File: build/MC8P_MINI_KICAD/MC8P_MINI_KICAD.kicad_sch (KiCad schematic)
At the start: 28 parts, among them J1 AudioJack3, SW1 ASSIGN, SW2 ENTER, SW3 PREV, SW4 NEXT, U1 CD74HC4067M

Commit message: production files
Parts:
- added R3, R4, R5, R6: 10k_0402, PCM_4ms_Resistor:R_0603, symbol PCM_4ms_Resistor:10k_0402
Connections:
- net 5V: now also SW1.1, SW2.1, SW3.1, SW4.1
- net ASSIGN: now also SW1.2, R3.1; no longer SW1.1
- net ENTER: now also SW2.2, R4.1; no longer SW2.1
- net GND: now also R3.2, R4.2, R5.2, R6.2; no longer SW1.2, SW2.2, SW3.2, SW4.2
- net NEXT: now also SW4.2, R5.1; no longer SW4.1
- net PREV: now also SW3.2, R6.1; no longer SW3.1
- no-connect marks 9 -> 22
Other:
- moved on the sheet: SW1, SW2, SW3, SW4

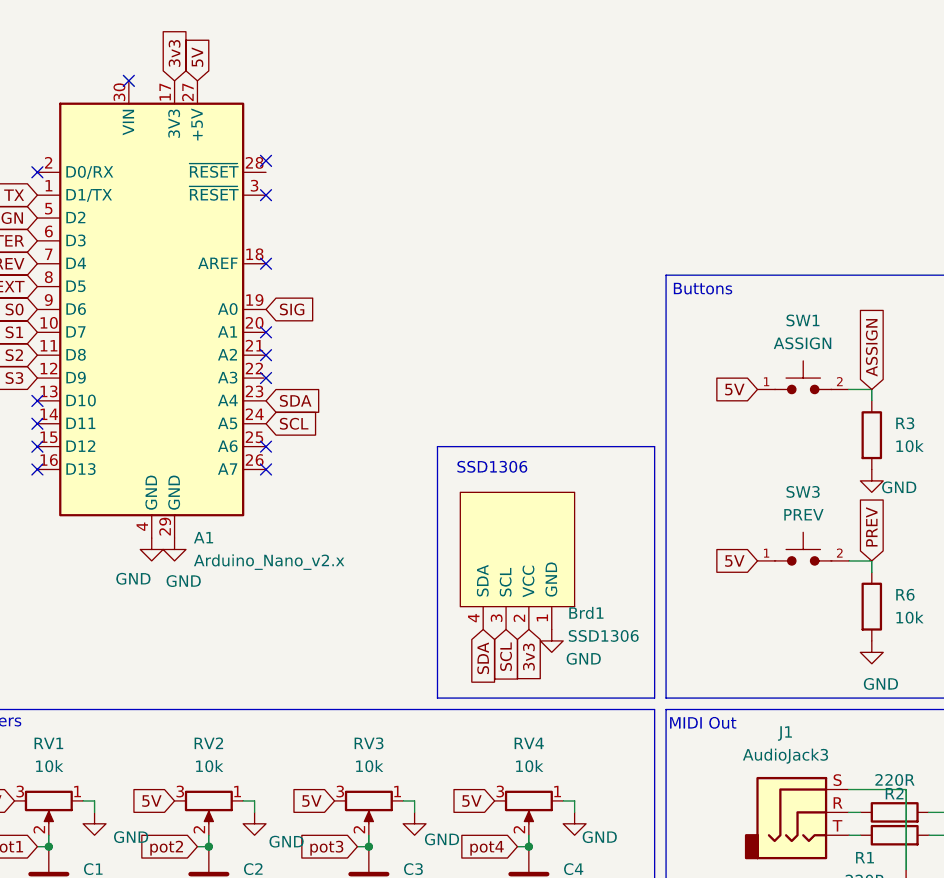
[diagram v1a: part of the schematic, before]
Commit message: PCB & Schematic Updated
Added pull up resistors with jumpers to work with Arduino nano r4
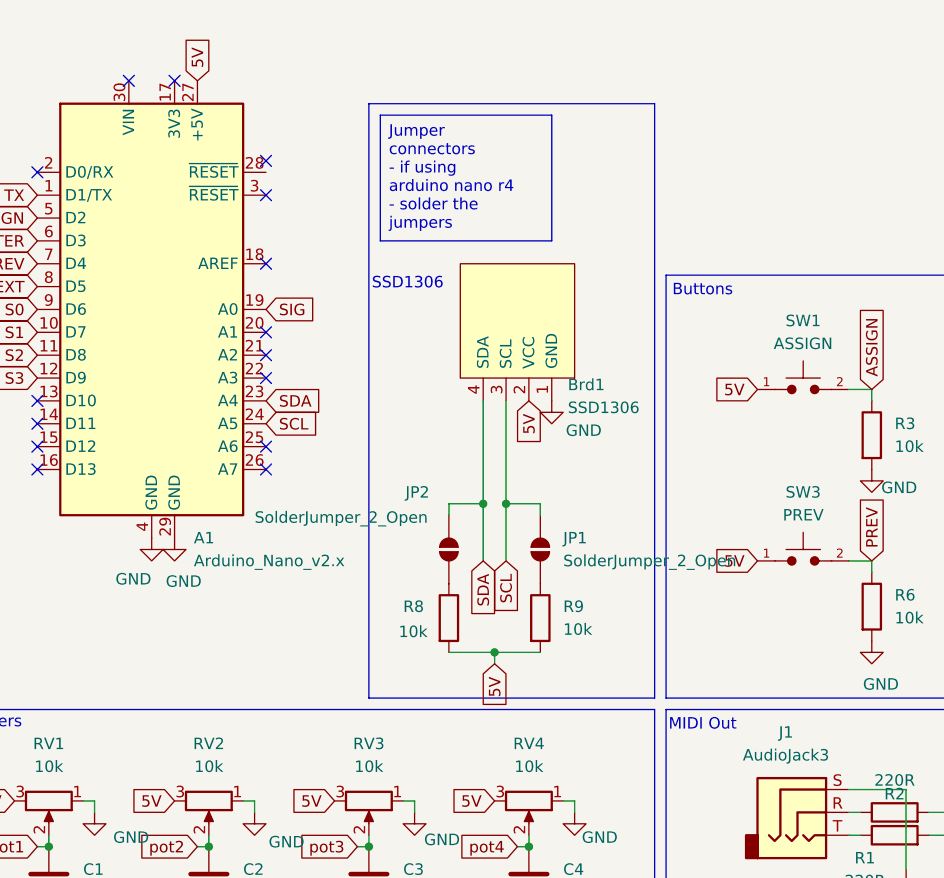
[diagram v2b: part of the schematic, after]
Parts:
- added JP1, JP2: SolderJumper_2_Open, Jumper:SolderJumper-2_P1.3mm_Open_RoundedPad1.0x1.5mm, symbol Jumper:SolderJumper_2_Open
- added R8, R9: 10k_0402, PCM_4ms_Resistor:R_0603, symbol PCM_4ms_Resistor:10k_0402
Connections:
- net 5V: now also Brd1.2 (VCC), R8.2, R9.2
- net SCL: now also JP1.2 (B)
- net SDA: now also JP2.2 (B)
- net 3v3: no longer names the net of A1.17 (3V3)
- net 3v3: no longer Brd1.2 (VCC)
- new net: JP1.1 (A), R9.1
- new net: JP2.1 (A), R8.1
- no-connect marks 22 -> 23
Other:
- moved on the sheet: Brd1

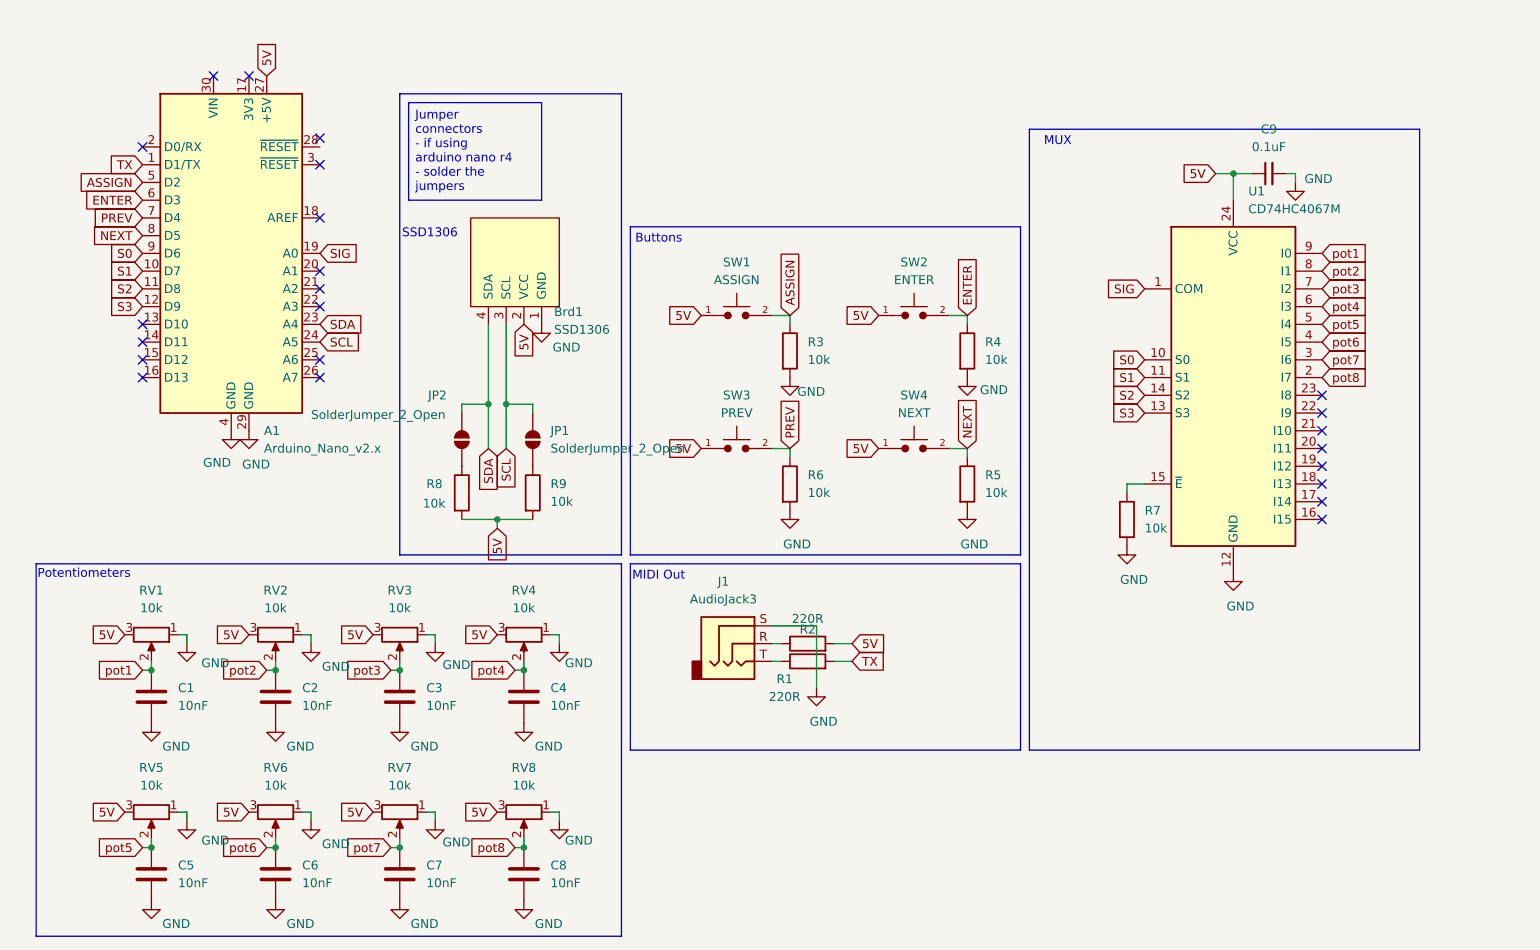
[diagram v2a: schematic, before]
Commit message: PCV Rev2
replaced Nano version with Pro Micro
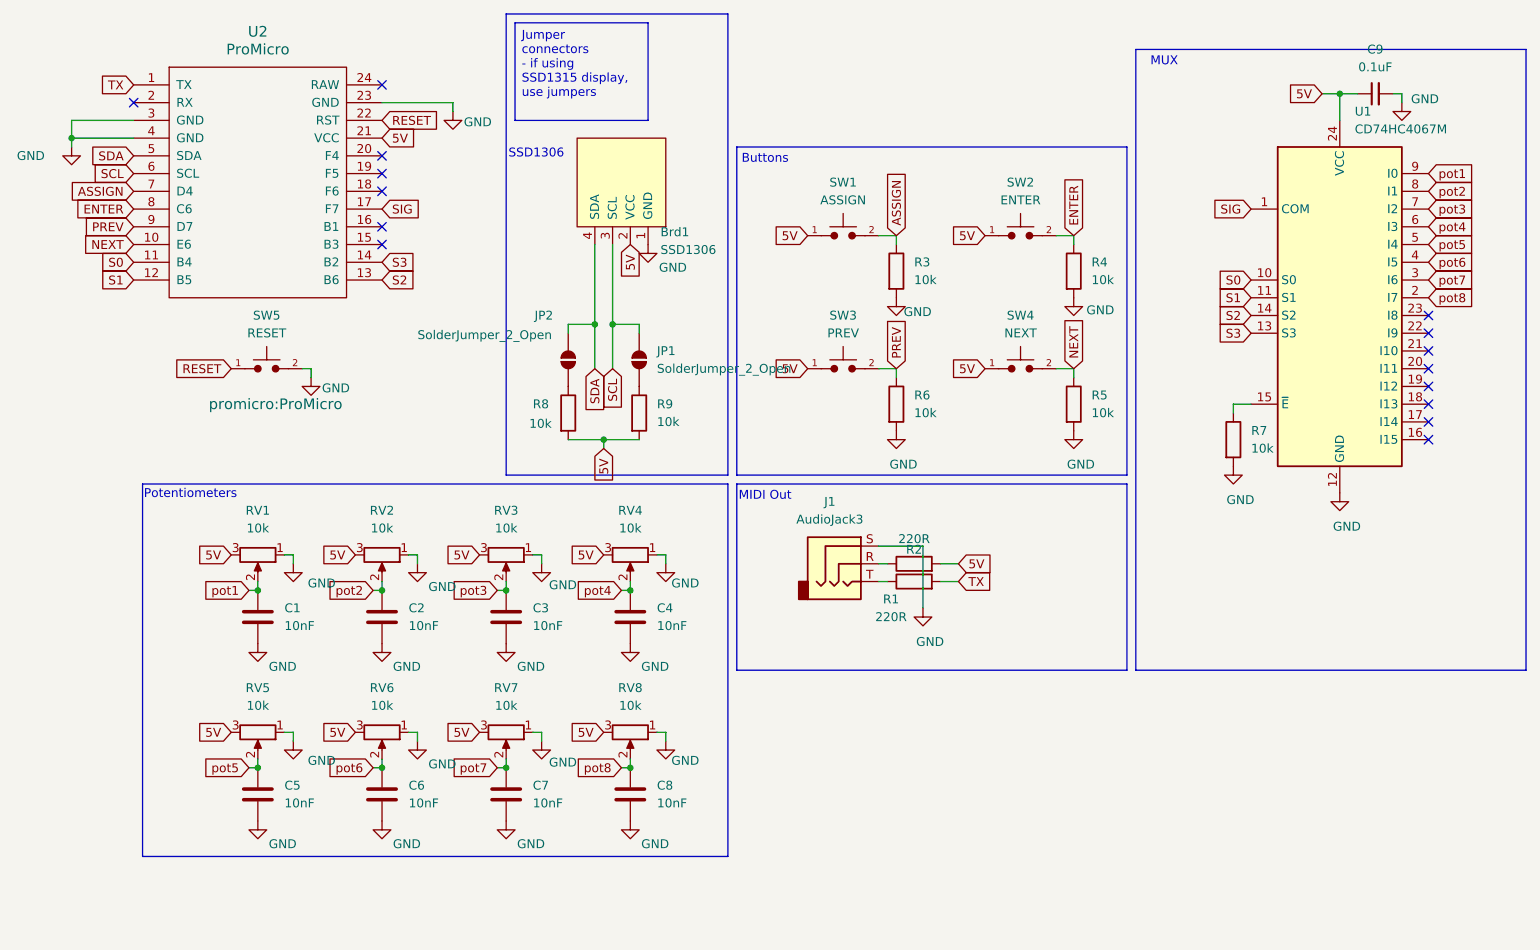
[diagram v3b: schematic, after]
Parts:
- removed A1: Arduino_Nano_v2.x, Module:Arduino_Nano, symbol MCU_Module:Arduino_Nano_v2.x
- added SW5: RESET, Button_Switch_SMD:SW_Push_1P1T_NO_CK_KMR2, symbol PCM_SL_Devices:Push_Button
- added U2: ProMicro, promicro:ProMicro, symbol promicro:ProMicro
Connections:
- net 5V: now also U2.21 (VCC)
- net ASSIGN: now also U2.7 (D4)
- net ENTER: now also U2.8 (C6)
- net GND: now also SW5.2, U2.23 (GND), U2.3 (GND), U2.4 (GND)
- net NEXT: now also U2.10 (E6)
- net PREV: now also U2.9 (D7)
- net S0: now also U2.11 (B4)
- net S1: now also U2.12 (B5)
- net S2: now also U2.13 (B6)
- net S3: now also U2.14 (B2)
- net SCL: now also U2.6 (SCL)
- net SDA: now also U2.5 (SDA)
- net SIG: now also U2.17 (F7)
- net TX: now also U2.1 (TX)
- new net RESET: SW5.1, U2.22 (RST)
- no-connect marks 23 -> 15
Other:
- moved on the sheet: Brd1, C1, C2, C3, C4, C5, C6, C7, C8, C9, J1, JP1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
